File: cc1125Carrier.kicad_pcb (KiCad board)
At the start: 2 copper layers, 65.9 x 78 mm, 5 parts, among them J1 TFM-110-02-SM-D-A-K-TR, J2 TFM-110-02-SM-D-A-K-TR, J3 Jumper Block, J4 Conn_01x06, U1 YAAJ_WeAct_BlackPill_Part_Lik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

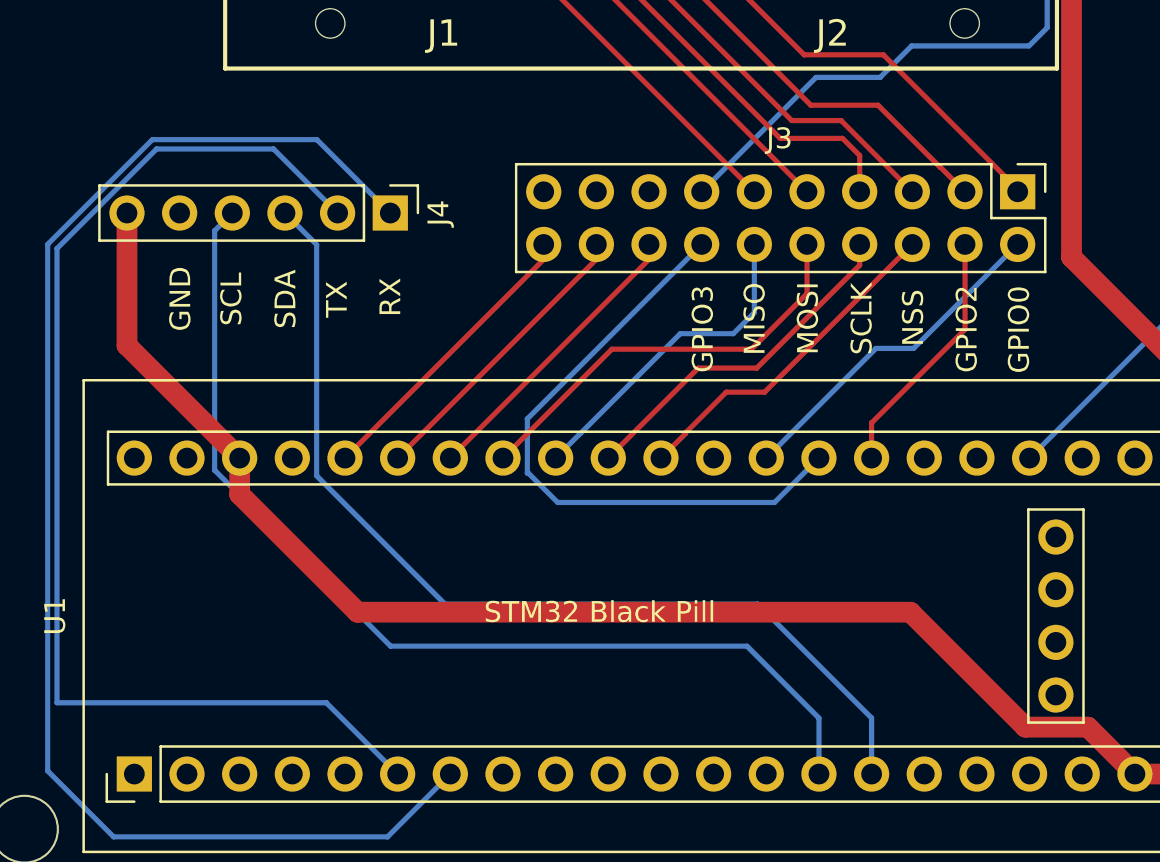
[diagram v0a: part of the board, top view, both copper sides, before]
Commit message: update pullups on i2c, update images
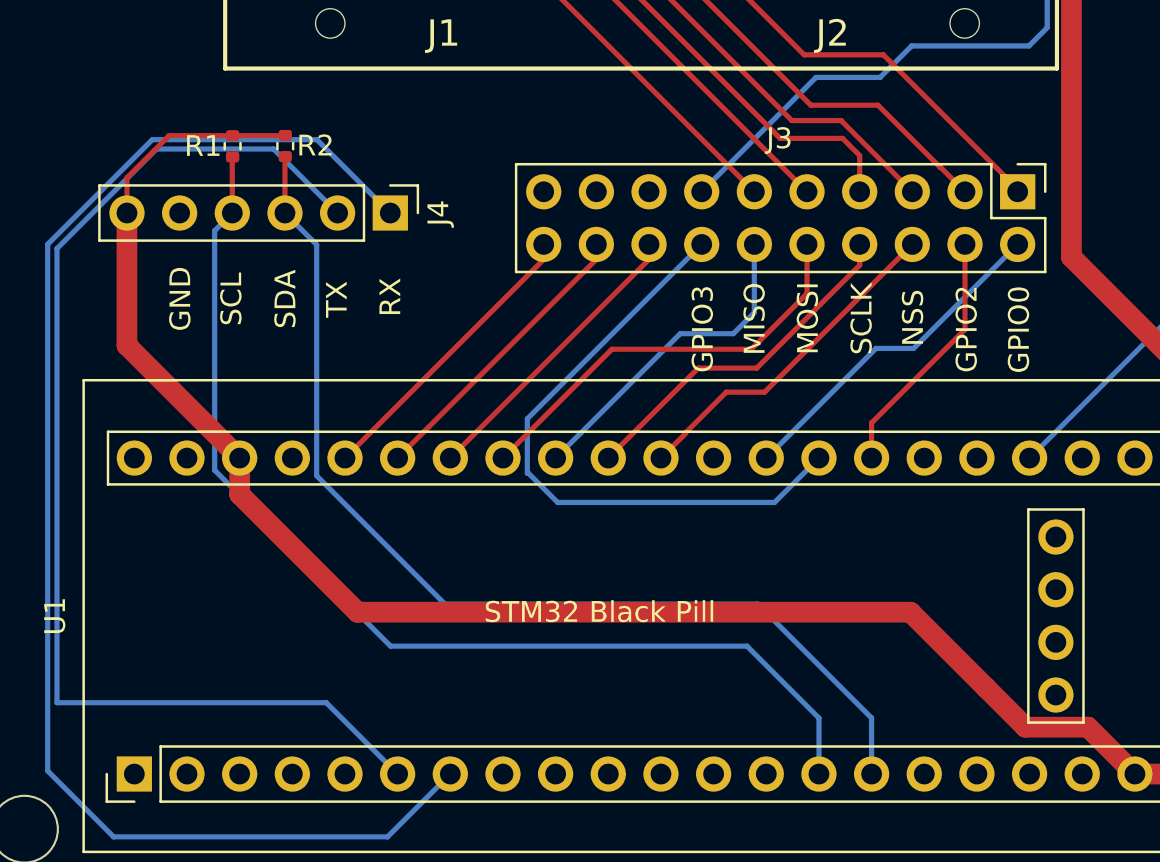
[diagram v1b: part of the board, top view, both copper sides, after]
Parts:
- added R1: 10k, Resistor_SMD:R_0402_1005Metric, F.Cu at (95.3, 104.8)
- added R2: 10k, Resistor_SMD:R_0402_1005Metric, F.Cu at (97.9, 104.8)
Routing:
- net MCU_VCC: track 150.2 -> 160.4 mm
- net SDA: track 47.6 -> 50.3 mm
- net SCL: track 49.6 -> 52.3 mm
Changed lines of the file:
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@@
+    )
+  )
+  (footprint "Resistor_SMD:R_0402_1005Metric" (layer "F.Cu")
+    (at 95.32 104.78 90)
+    (descr "Resistor SMD 0402 (1005 Metric), square (rectangular) end terminal, IPC_7351 nominal, (Body size source: IPC-SM-782 page 72, https://www.pcb-3d.com/wordpress/wp-content/uploads/ipc-sm-782a_amendment_1_and_2.pdf), generated with kicad-footprint-generator")
+    (tags "resistor")
+    (property "Sheetfile" "cc1125Carrier.kicad_sch")
+    (property "Sheetname" "")
+    (attr smd)
+    (fp_text reference "R1" (at 0 -1.42) (layer "F.SilkS")
+      (effects (font (size 1 1) (thickness 0.15)))
+    )
+    (fp_text value "10k" (at 1.74 -0.09) (layer "F.Fab")
+      (effects (font (size 1 1) (thickness 0.15)))
+    )
+    (fp_text user "${REFERENCE}" (at 0 0 90) (layer "F.Fab")
+      (effects (font (size 0.26 0.26) (thickness 0.04)))
+    )
+    (fp_line (start -0.153641 0.38) (end 0.153641 0.38) (layer "F.SilkS") (width 0.12))
+    (fp_line (start -0.153641 -0.38) (end 0.153641 -0.38) (layer "F.SilkS") (width 0.12))
+    (fp_line (start -0.93 -0.47) (end 0.93 -0.47) (layer "F.CrtYd") (width 0.05))
+    (fp_line (start -0.93 0.47) (end -0.93 -0.47) (layer "F.CrtYd") (width 0.05))
+    (fp_line (start 0.93 -0.47) (end 0.93 0.47) (layer "F.CrtYd") (width 0.05))
+    (fp_line (start 0.93 0.47) (end -0.93 0.47) (layer "F.CrtYd") (width 0.05))
+    (fp_line (start 0.525 -0.27) (end 0.525 0.27) (layer "F.Fab") (width 0.1))
+    (fp_line (start -0.525 -0.27) (end 0.525 -0.27) (layer "F.Fab") (width 0.1))
+    (fp_line (start 0.525 0.27) (end -0.525 0.27) (layer "F.Fab") (width 0.1))
+    (fp_line (start -0.525 0.27) (end -0.525 -0.27) (layer "F.Fab") (width 0.1))
+    (pad "1" smd roundrect (at -0.51 0 90) (size 0.54 0.64) (layers "F.Cu" "F.Paste" "F.Mask") (roundrect_rratio 0.25)
+      (net 79 "SCL") (pintype "passive"))
+    (pad "2" smd roundrect (at 0.51 0 90) (size 0.54 0.64) (layers "F.Cu" "F.Paste" "F.Mask") (roundrect_rratio 0.25)
+      (net 51 "MCU_VCC") (pintype "passive"))
+    (model "${KICAD6_3DMODEL_DIR}/Resistor_SMD.3dshapes/R_0402_1005Metric.wrl"
+      (offset (xyz 0 0 0))
+      (scale (xyz 1 1 1))
+      (rotate (xyz 0 0 0))
+    )
+  )
+  (footprint "Resistor_SMD:R_0402_1005Metric" (layer "F.Cu")
+    (at 97.86 104.77 90)
+    (descr "Resistor SMD 0402 (1005 Metric), square (rectangular) end terminal, IPC_7351 nominal, (Body size source: IPC-SM-782 page 72, https://www.pcb-3d.com/wordpress/wp-content/uploads/ipc-sm-782a_amendment_1_and_2.pdf), generated with kicad-footprint-generator")
+    (tags "resistor")
+    (property "Sheetfile" "cc1125Carrier.kicad_sch")
+    (property "Sheetname" "")
+    (attr smd)
+    (fp_text reference "R2" (at 0.01 1.46) (layer "F.SilkS")
+      (effects (font (size 1 1) (thickness 0.15)))
+    )
+    (fp_text value "10k" (at 1.79 0.48) (layer "F.Fab")
+      (effects (font (size 1 1) (thickness 0.15)))
+    )
+    (fp_text user "${REFERENCE}" (at 0 0 90) (layer "F.Fab")
+      (effects (font (size 0.26 0.26) (thickness 0.04)))
+    )
+    (fp_line (start -0.153641 0.38) (end 0.153641 0.38) (layer "F.SilkS") (width 0.12))
+    (fp_line (start -0.153641 -0.38) (end 0.153641 -0.38) (layer "F.SilkS") (width 0.12))
+    (fp_line (start 0.93 -0.47) (end 0.93 0.47) (layer "F.CrtYd") (width 0.05))
+    (fp_line (start -0.93 -0.47) (end 0.93 -0.47) (layer "F.CrtYd") (width 0.05))
+    (fp_line (start -0.93 0.47) (end -0.93 -0.47) (layer "F.CrtYd") (width 0.05))
+    (fp_line (start 0.93 0.47) (end -0.93 0.47) (layer "F.CrtYd") (width 0.05))
+    (fp_line (start 0.525 0.27) (end -0.525 0.27) (layer "F.Fab") (width 0.1))
+    (fp_line (start 0.525 -0.27) (end 0.525 0.27) (layer "F.Fab") (width 0.1))
+    (fp_line (start -0.525 -0.27) (end 0.525 -0.27) (layer "F.Fab") (width 0.1))
+    (fp_line (start -0.525 0.27) (end -0.525 -0.27) (layer "F.Fab") (width 0.1))
+    (pad "1" smd roundrect (at -0.51 0 90) (size 0.54 0.64) (layers "F.Cu" "F.Paste" "F.Mask") (roundrect_rratio 0.25)
+      (net 78 "SDA") (pintype "passive"))
+    (pad "2" smd roundrect (at 0.51 0 90) (size 0.54 0.64) (layers "F.Cu" "F.Paste" "F.Mask") (roundrect_rratio 0.25)
+      (net 51 "MCU_VCC") (pintype "passive"))
+    (model "${KICAD6_3DMODEL_DIR}/Resistor_SMD.3dshapes/R_0402_1005Metric.wrl"
+      (offset (xyz 0 0 0))
+      (scale (xyz 1 1 1))
+      (rotate (xyz 0 0 0))
     )
   )
@@
   (segment (start 123.6 119.82) (end 121.46 121.96) (width 0.25) (layer "B.Cu") (net 28))
   (segment (start 135.78 110.126) (end 141.986 116.332) (width 1) (layer "F.Cu") (net 51))
-  (segment (start 133.559511 132.797511) (end 128.016 127.254) (width 1) (layer "F.Cu") (net 51))
+  (segment (start 133.559511 132.797511) (end 131.666 130.904) (width 1) (layer "F.Cu") (net 51))
   (segment (start 124.59 82.23) (end 125.43 81.39) (width 1) (layer "F.Cu") (net 51))
   (segment (start 128.915 90.915) (end 128.915 92.185) (width 1) (layer "F.Cu") (net 51))
+  (segment (start 97.85 104.27) (end 97.86 104.26) (width 0.25) (layer "F.Cu") (net 51))
   (segment (start 126.925 90.915) (end 124.59 88.58) (width 1) (layer "F.Cu") (net 51))
+  (segment (start 95.32 104.27) (end 92.96 104.27) (width 0.25) (layer "F.Cu") (net 51))
   (segment (start 126.925 90.915) (end 126.925 91.735) (width 1) (layer "F.Cu") (net 51))
+  (segment (start 131.666 130.904) (end 128.016 127.254) (width 1) (layer "F.Cu") (net 51))
   (segment (start 95.66 121.568) (end 95.66 119.82) (width 1) (layer "F.Cu") (net 51))
   (segment (start 125.43 81.39) (end 134.9 81.39) (width 1) (layer "F.Cu") (net 51))
   (segment (start 136.577511 132.797511) (end 133.559511 132.797511) (width 1) (layer "F.Cu") (net 51))
+  (segment (start 92.25 104.27) (end 90.225 106.295) (width 0.25) (layer "F.Cu") (net 51))
   (segment (start 135.78 82.38) (end 135.78 110.126) (width 1) (layer "F.Cu") (net 51))
   (segment (start 90.225 114.385) (end 90.225 108) (width 1) (layer "F.Cu") (net 51))
   (segment (start 95.66 119.82) (end 90.225 114.385) (width 1) (layer "F.Cu") (net 51))
   (segment (start 135.835 82.325) (end 135.78 82.38) (width 1) (layer "F.Cu") (net 51))
+  (segment (start 95.32 104.27) (end 97.85 104.27) (width 0.25) (layer "F.Cu") (net 51))
   (segment (start 124.59 88.58) (end 124.59 82.23) (width 1) (layer "F.Cu") (net 51))
   (segment (start 141.986 133.858) (end 140.784 135.06) (width 1) (layer "F.Cu") (net 51))
   (segment (start 126.925 90.915) (end 128.915 90.915) (width 1) (layer "F.Cu") (net 51))
   (segment (start 140.784 135.06) (end 138.84 135.06) (width 1) (layer "F.Cu") (net 51))
+  (segment (start 92.96 104.27) (end 92.25 104.27) (width 0.25) (layer "F.Cu") (net 51))
   (segment (start 138.84 135.06) (end 136.577511 132.797511) (width 1) (layer "F.Cu") (net 51))
   (segment (start 141.986 116.332) (end 141.986 133.858) (width 1) (layer "F.Cu") (net 51))
   (segment (start 134.9 81.39) (end 135.835 82.325) (width 1) (layer "F.Cu") (net 51))
+  (segment (start 90.225 106.295) (end 90.225 108) (width 0.25) (layer "F.Cu") (net 51))
   (segment (start 101.346 127.254) (end 95.66 121.568) (width 1) (layer "F.Cu") (net 51))
   (segment (start 128.016 127.254) (end 101.346 127.254) (width 1) (layer "F.Cu") (net 51))
@@
   (segment (start 99.84 131.62) (end 86.85 131.62) (width 0.25) (layer "B.Cu") (net 77))
   (segment (start 91.65399 104.91) (end 86.85 109.71399) (width 0.25) (layer "B.Cu") (net 77))
+  (segment (start 97.86 105.28) (end 97.845 105.295) (width 0.25) (layer "F.Cu") (net 78))
+  (segment (start 97.845 105.295) (end 97.845 108) (width 0.25) (layer "F.Cu") (net 78))
   (segment (start 126.14 132.36) (end 126.14 135.06) (width 0.25) (layer "B.Cu") (net 78))
   (segment (start 120.64 126.86) (end 126.14 132.36) (width 0.25) (layer "B.Cu") (net 78))
@@
   (segment (start 97.845 108) (end 99.374511 109.529511) (width 0.25) (layer "B.Cu") (net 78))
   (segment (start 99.374511 120.674511) (end 105.56 126.86) (width 0.25) (layer "B.Cu") (net 78))
+  (segment (start 95.32 105.29) (end 95.305 105.305) (width 0.25) (layer "F.Cu") (net 79))
+  (segment (start 95.305 105.305) (end 95.305 108) (width 0.25) (layer "F.Cu") (net 79))
   (segment (start 120.13 128.89) (end 123.6 132.36) (width 0.25) (layer "B.Cu") (net 79))
-  (segment (start 123.6 132.36) (end 123.6 135.06) (width 0.25) (layer "B.Cu") (net 79))
   (segment (start 95.305 108) (end 94.455 108.85) (width 0.25) (layer "B.Cu") (net 79))
   (segment (start 94.455 108.85) (end 94.455 120.405) (width 0.25) (layer "B.Cu") (net 79))
   (segment (start 102.94 128.89) (end 120.13 128.89) (width 0.25) (layer "B.Cu") (net 79))
+  (segment (start 123.6 132.36) (end 123.6 135.06) (width 0.25) (layer "B.Cu") (net 79))
   (segment (start 94.455 120.405) (end 102.94 128.89) (width 0.25) (layer "B.Cu") (net 79))
   (zone (net 1) (net_name "GND") (layers F&B.Cu) (hatch edge 0.508)

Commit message: minor board tweaks
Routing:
- net RX: track 67.5 -> 75.5 mm
- net TX: track 56.6 -> 64.6 mm
- net NRST: track 38.1 -> 45.9 mm
- net SCL: track 52.3 -> 56.2 mm
- net MCU_VCC: track 160.4 -> 162.4 mm
- net MISO: track 15.8 -> 14.3 mm
- net GND: vias 3 -> 1
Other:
- board text added: "3.3V"
- board text added: "Cross to connect Black Pill Use top of the block to connect to CC112X"
- board text added: "Ext PWR"
- board text added: "I2C"
- board text added: "UART"
